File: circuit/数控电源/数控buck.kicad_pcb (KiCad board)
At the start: 2 copper layers, 56.4 x 40.5 mm, 81 parts, among them J1 Conn_01x06_MountingPin, J2 Conn_01x02, J5 Conn_01x02, Q1 BSC070N10NS3G, Q2 BSC070N10NS3G, SW1 SW_Push, U1 STM32F334R8Tx, U2 LM5164DDA, U3 TLV9062, U4 LM5109MA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

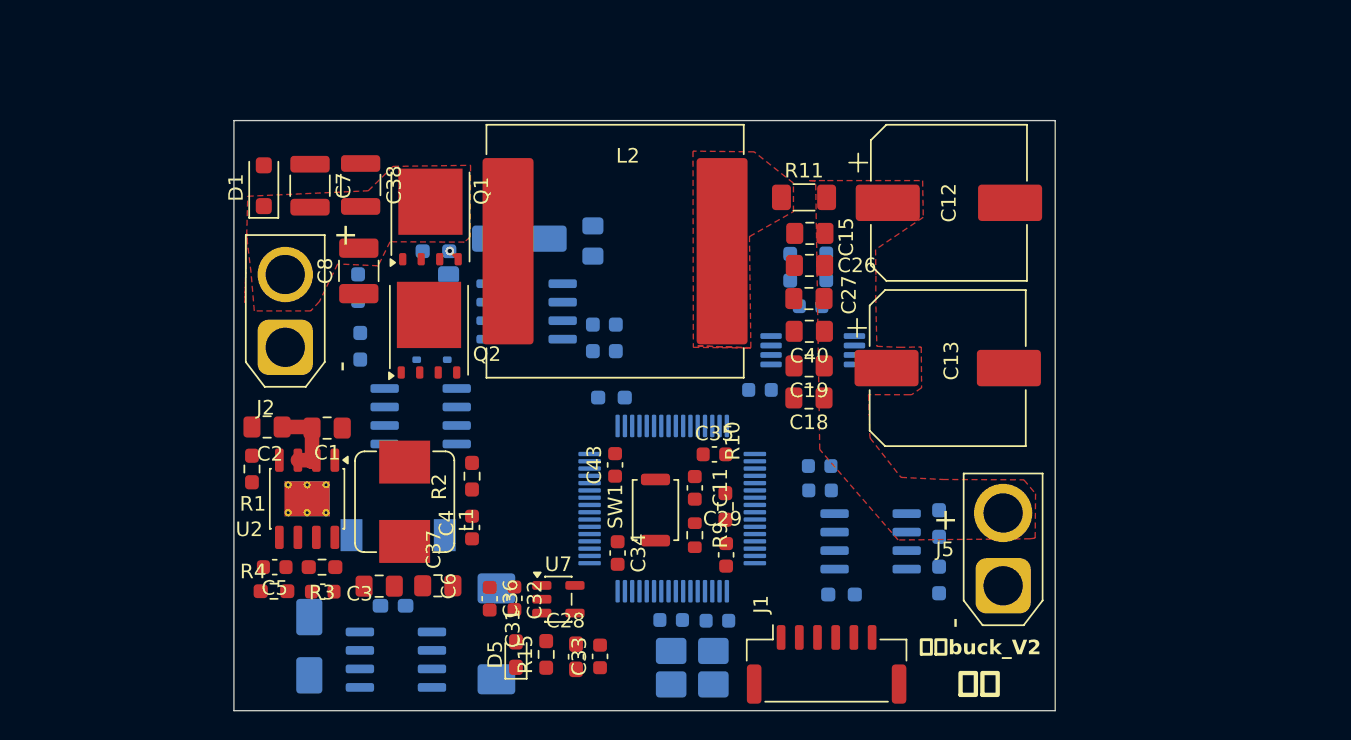
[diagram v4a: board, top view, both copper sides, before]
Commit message: 重新对第二版pcb进行布局
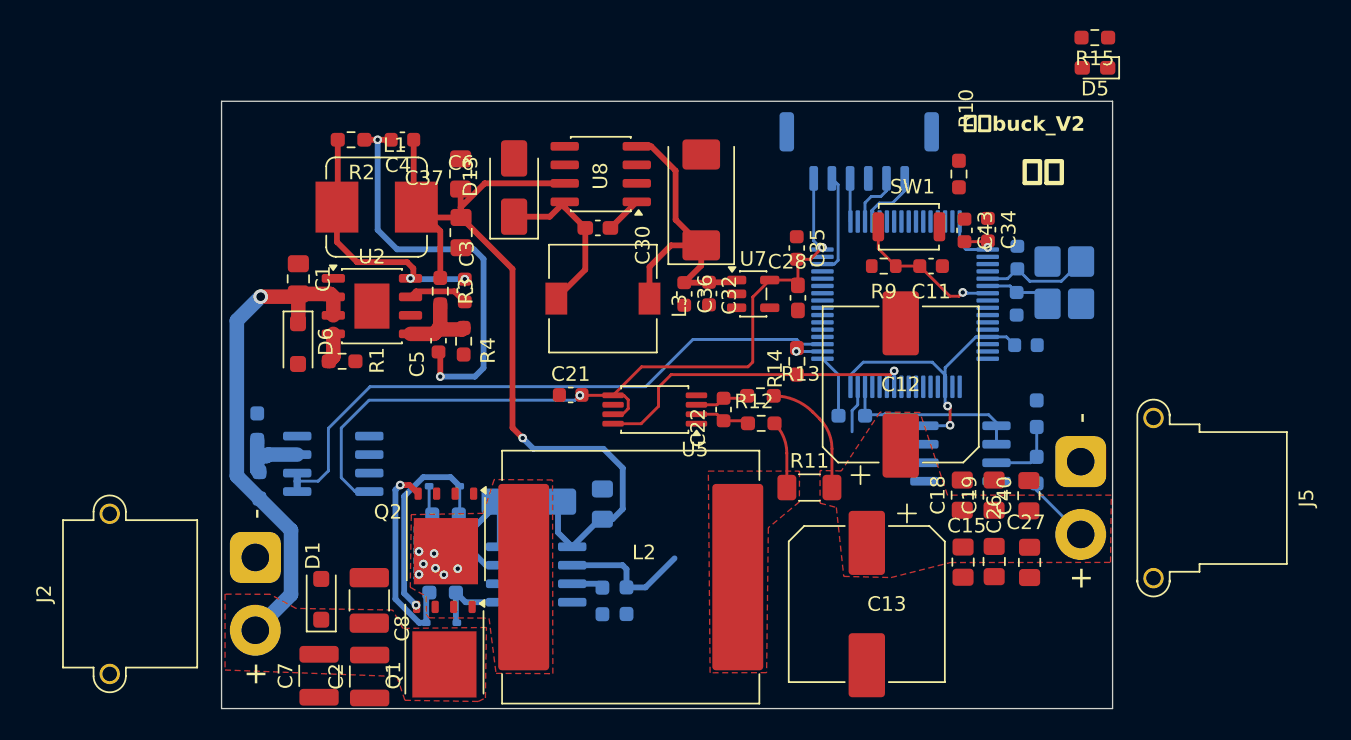
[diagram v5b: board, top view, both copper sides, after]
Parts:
- removed C24, C29: 100n, Capacitor_SMD:C_0603_1608Metric
- removed C38: 10u, Capacitor_SMD:C_1210_3225Metric
- added D6: SMCJ58A, Diode_SMD:D_SOD-123F, F.Cu at (19.1, 54.1)
- C2: value 22u -> 10u; footprint Capacitor_SMD:C_0805_2012Metric_Pad1.18x1.45mm_HandSolder -> Capacitor_SMD:C_1210_3225Metric
- C21, C22, C30, C31, D13, L3, R12, R13, R14, U5, U8: moved to F.Cu
- C33, J1: moved to B.Cu
- J2: footprint Connector_AMASS:AMASS_XT30U-M_1x02_P5.0mm_Vertical -> Connector_AMASS:AMASS_XT30PW-M_1x02_P2.50mm_Horizontal
- J5: footprint Connector_AMASS:AMASS_XT30U-F_1x02_P5.0mm_Vertical -> Connector_AMASS:AMASS_XT30PW-F_1x02_P2.50mm_Horizontal
- R2: value 11k -> 453k
- U2: footprint Package_SO:HSOP-8-1EP_3.9x4.9mm_P1.27mm_EP2.41x3.1mm_ThermalVias -> Package_SO:HSOP-8-1EP_3.9x4.9mm_P1.27mm_EP2.41x3.1mm
- moved R15 56.7 mm to (73.9, 33.1), turned to 180 degrees
- moved D5 56.6 mm to (73.9, 35.2), turned to 180 degrees
- moved Y1 36.8 mm to (71.8, 50.0), turned to -90 degrees
- moved C33 36.2 mm to (69.1, 54.2), turned to 180 degrees
- moved U8 36.2 mm to (39.9, 42.5)
- moved J1 35.3 mm to (57.7, 41.0)
- moved D13 34.5 mm to (34.0, 43.4), turned to 90 degrees
- moved C34 33.8 mm to (66.5, 46.3)
- moved C7 33.7 mm to (20.6, 77.0), turned to 90 degrees
- moved C31 33.0 mm to (46.8, 44.3), turned to 90 degrees
- moved C14 32.3 mm to (68.5, 48.2), turned to -90 degrees
- moved C16 32.2 mm to (68.5, 51.4), turned to 90 degrees
- moved Q1 29.7 mm to (29.2, 75.1), turned to -90 degrees
- moved C30 29.5 mm to (39.7, 46.2)
- moved C28 29.0 mm to (53.5, 51.0)
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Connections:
- C2 pad 1: +48V -> GND
- C2 pad 2: GND -> +48V
- C25 pad 1: Net-(C24-Pad1) -> GND
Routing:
- net +3.3V: track 0.00 -> 84.3 mm, vias 0 -> 5
- net +12V: track 0.00 -> 58.9 mm, vias 0 -> 1
- net /adc_Vin: track 0.00 -> 43.2 mm
- net +48V: track 5.38 -> 34.6 mm, vias 0 -> 1
- net Net-(C4-Pad1): track 0.00 -> 28.6 mm, vias 0 -> 2
- net /comp_cirurt: track 0.00 -> 22.7 mm, vias 0 -> 1
- net +5V: track 0.00 -> 22.3 mm
- net Net-(U2-SW): track 0.00 -> 17.6 mm, vias 0 -> 2
- net Net-(D4-A): track 0.00 -> 14.4 mm, vias 0 -> 1
- net Net-(D3-A): track 0.81 -> 14.5 mm
- net +24V: track 0.00 -> 13.3 mm
- net /comp_volt: track 0.00 -> 12.8 mm
- net Net-(D13-K): track 0.00 -> 12.0 mm
- net /NRST: track 0.00 -> 10.5 mm, vias 0 -> 1
- net /HRTIM_+: track 0.00 -> 9.22 mm
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- added copper zone on B.Cu, net Net-(Q2-D)
- added copper zone on F.Cu, net Net-(Q2-D)
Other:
- board size 56.4 x 40.5 mm -> 61.2 x 41.7 mm

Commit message: 完成连线，还有几个报错
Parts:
- moved R15 25.8 mm to (50.5, 44.1), turned to -90 degrees
- moved D5 23.1 mm to (52.6, 44.1), turned to -90 degrees
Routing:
- net /HRTIM_-: track 2.19 -> 36.2 mm, vias 0 -> 2
- net +3.3V: track 84.3 -> 116.7 mm, vias 5 -> 6
- net /HRTIM_+: track 9.22 -> 35.4 mm, vias 0 -> 2
- net GND: track 3.25 -> 21.4 mm, vias 0 -> 568
- net /BOOT0: track 0.00 -> 3.96 mm, vias 0 -> 1
- net Net-(Q2-D): track 0.00 -> 3.34 mm
- net Net-(D5-A): track 0.00 -> 2.81 mm
- net +24V: track 13.3 -> 12.4 mm, vias 0 -> 2
- net /USART3_RX: track 4.44 -> 5.20 mm
- net Net-(L2-Pad2): vias 0 -> 2
- added copper zone on B.Cu, net GND
- added copper zone on F.Cu, net GND
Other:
- board size 61.2 x 41.7 mm -> 61.6 x 42.1 mm

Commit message: 完成pcb
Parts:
- removed C32: 100nf, Capacitor_SMD:C_0603_1608Metric
- added G***: LOGO, LOGO, B.Cu at (29.0, 48.4)
- moved C36 1.53 mm to (47.2, 50.8)
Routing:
- net GND: track 21.4 -> 33.9 mm, vias 568 -> 570
- net +5V: track 22.3 -> 23.6 mm
